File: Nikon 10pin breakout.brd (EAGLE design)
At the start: 14.5 x 26 mm, 2 parts, among them J1 10p-2.54

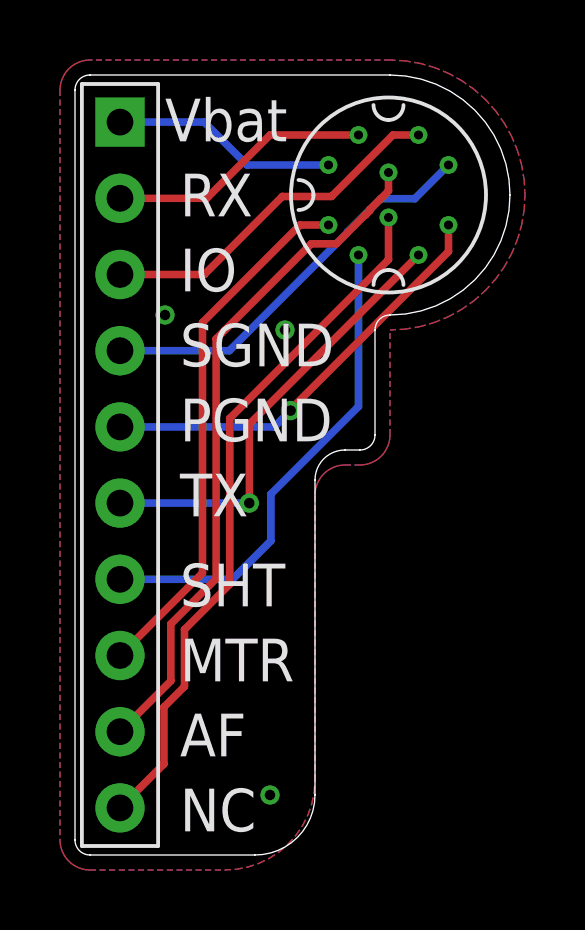
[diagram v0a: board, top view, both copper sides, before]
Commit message: - corrected routing neat the PCB edge
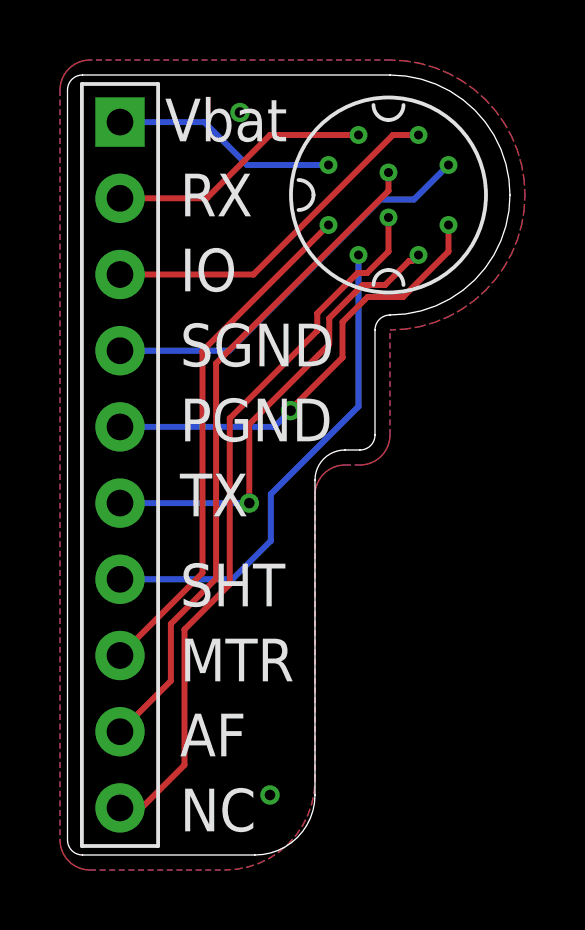
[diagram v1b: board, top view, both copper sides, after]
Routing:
- net POWER_GND: track 14.3 -> 15.0 mm
- net NC: track 23.4 -> 24.0 mm
- net METER: track 17.8 -> 17.2 mm
- net TX: track 14.9 -> 15.4 mm
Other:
- board size 14.5 x 26 mm -> 14.8 x 26 mm
